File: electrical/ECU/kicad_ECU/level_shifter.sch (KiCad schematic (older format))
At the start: 24 parts

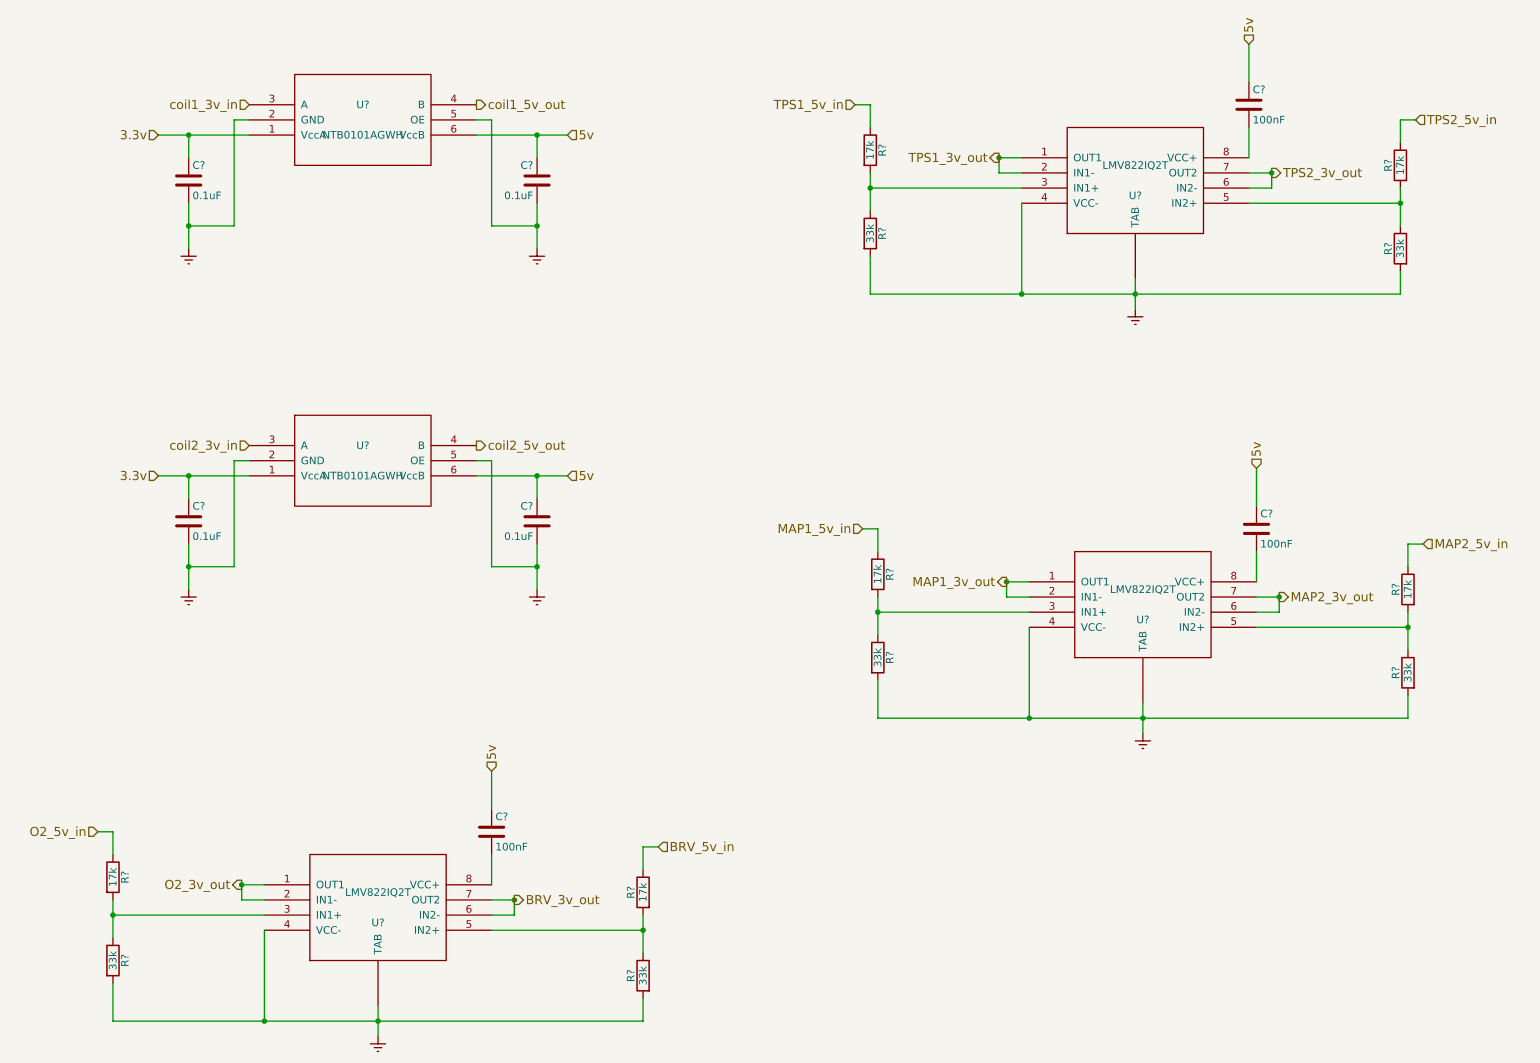
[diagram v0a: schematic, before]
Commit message: fixed some naming errors and initial round of double checking
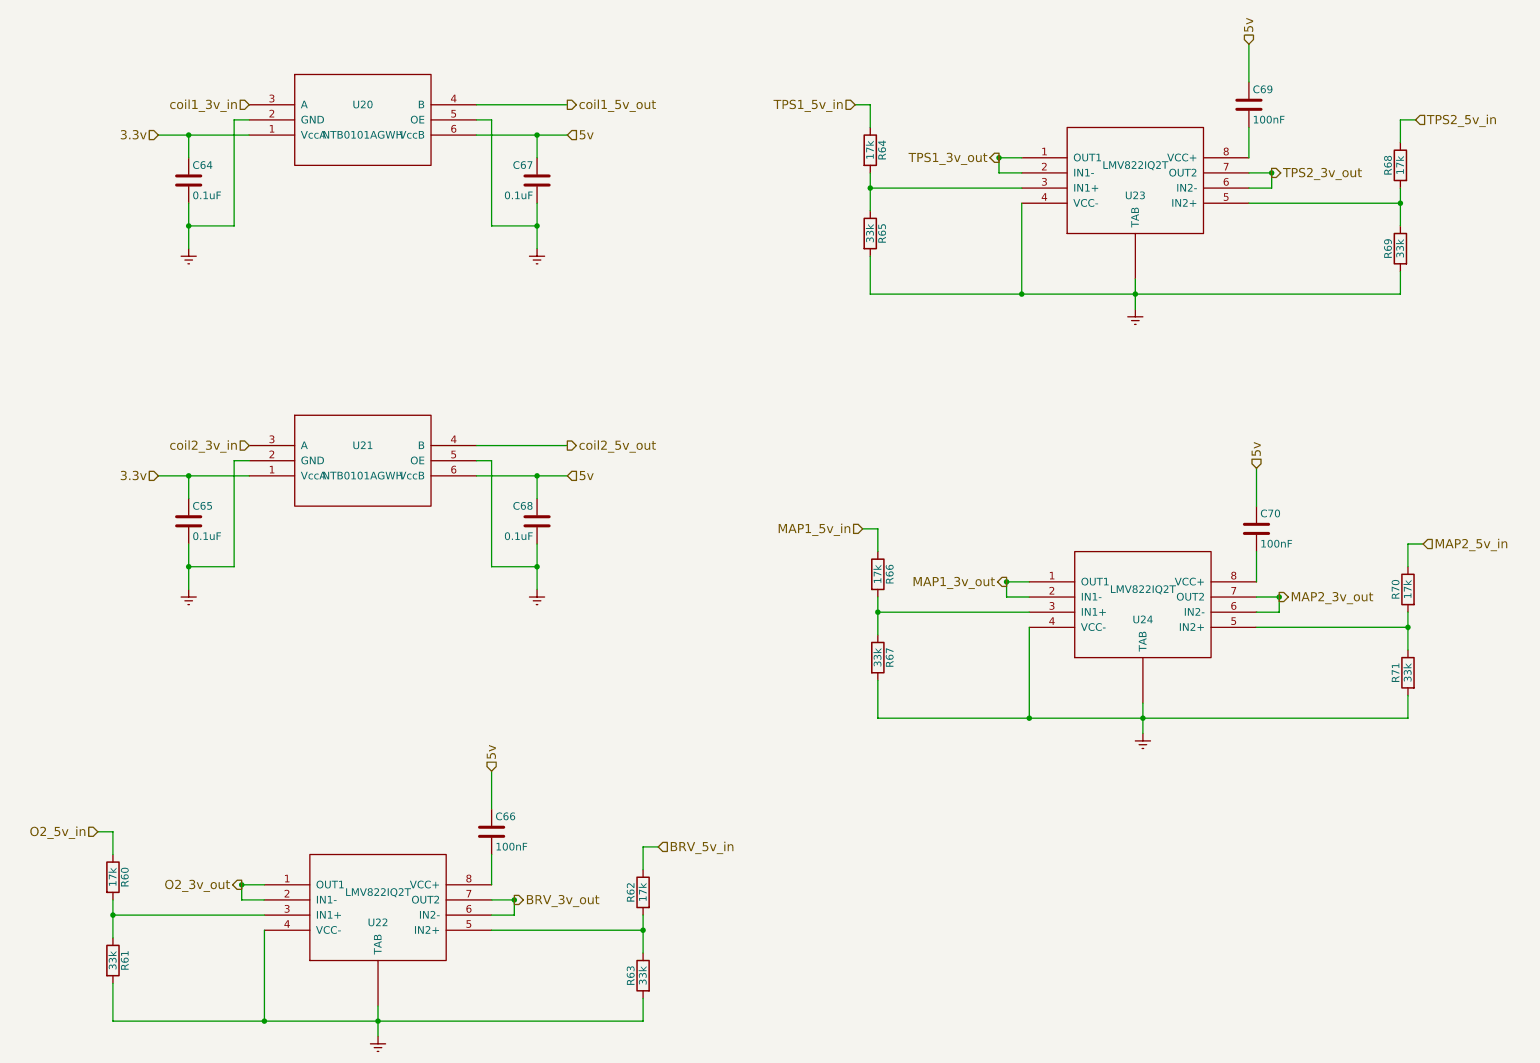
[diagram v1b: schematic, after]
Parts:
- gave numbers to parts that had none: 24
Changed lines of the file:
@@
 $Descr A4 11693 8268
 encoding utf-8
-Sheet 21 33
+Sheet 25 33
 Title "Level shifter 3.3v <-> 5v"
 Date ""
@@
 Text HLabel 9400 1650 2    60   Output ~ 0
 TPS2_3v_out
-Text HLabel 4150 1200 2    60   Output ~ 0
+Text HLabel 4750 1200 2    60   Output ~ 0
 coil1_5v_out
-Text HLabel 4150 3450 2    60   Output ~ 0
+Text HLabel 4750 3450 2    60   Output ~ 0
 coil2_5v_out
 $Comp
-L LMV822IQ2T U?
+L LMV822IQ2T U23
 U 1 1 597915F5
 P 8500 1700
-F 0 "U?" H 8500 1600 50  0000 C CNN
+F 0 "U23" H 8500 1600 50  0000 C CNN
 F 1 "LMV822IQ2T" H 8500 1800 50  0000 C CNN
 F 2 "MODULE" H 8500 1700 50  0001 C CNN
@@
 $EndComp
 $Comp
-L Earth #PWR?
+L Earth #PWR64
 U 1 1 597916F8
 P 8500 2550
-F 0 "#PWR?" H 8500 2300 50  0001 C CNN
+F 0 "#PWR64" H 8500 2300 50  0001 C CNN
 F 1 "Earth" H 8500 2400 50  0001 C CNN
 F 2 "" H 8500 2550 50  0001 C CNN
@@
 $EndComp
 $Comp
-L R R?
+L R R64
 U 1 1 59791774
 P 6750 1500
-F 0 "R?" V 6830 1500 50  0000 C CNN
+F 0 "R64" V 6830 1500 50  0000 C CNN
 F 1 "17k" V 6750 1500 50  0000 C CNN
 F 2 "" V 6680 1500 50  0001 C CNN
@@
 $EndComp
 $Comp
-L R R?
+L R R65
 U 1 1 5979178D
 P 6750 2050
-F 0 "R?" V 6830 2050 50  0000 C CNN
+F 0 "R65" V 6830 2050 50  0000 C CNN
 F 1 "33k" V 6750 2050 50  0000 C CNN
 F 2 "" V 6680 2050 50  0001 C CNN
@@
 $EndComp
 $Comp
-L C C?
+L C C69
 U 1 1 597917D3
 P 9250 1200
-F 0 "C?" H 9275 1300 50  0000 L CNN
+F 0 "C69" H 9275 1300 50  0000 L CNN
 F 1 "100nF" H 9275 1100 50  0000 L CNN
 F 2 "" H 9288 1050 50  0001 C CNN
@@
 Connection ~ 7750 2450
 $Comp
-L R R?
+L R R68
 U 1 1 59791914
 P 10250 1600
-F 0 "R?" V 10330 1600 50  0000 C CNN
+F 0 "R68" V 10330 1600 50  0000 C CNN
 F 1 "17k" V 10250 1600 50  0000 C CNN
 F 2 "" V 10180 1600 50  0001 C CNN
@@
 $EndComp
 $Comp
-L R R?
+L R R69
 U 1 1 5979191A
 P 10250 2150
-F 0 "R?" V 10330 2150 50  0000 C CNN
+F 0 "R69" V 10330 2150 50  0000 C CNN
 F 1 "33k" V 10250 2150 50  0000 C CNN
 F 2 "" V 10180 2150 50  0001 C CNN
@@
 MAP2_3v_out
 $Comp
-L LMV822IQ2T U?
+L LMV822IQ2T U24
 U 1 1 59791C46
 P 8550 4500
-F 0 "U?" H 8550 4400 50  0000 C CNN
+F 0 "U24" H 8550 4400 50  0000 C CNN
 F 1 "LMV822IQ2T" H 8550 4600 50  0000 C CNN
 F 2 "MODULE" H 8550 4500 50  0001 C CNN
@@
 $EndComp
 $Comp
-L Earth #PWR?
+L Earth #PWR65
 U 1 1 59791C4C
 P 8550 5350
-F 0 "#PWR?" H 8550 5100 50  0001 C CNN
+F 0 "#PWR65" H 8550 5100 50  0001 C CNN
 F 1 "Earth" H 8550 5200 50  0001 C CNN
 F 2 "" H 8550 5350 50  0001 C CNN
@@
 $EndComp
 $Comp
-L R R?
+L R R66
 U 1 1 59791C52
 P 6800 4300
-F 0 "R?" V 6880 4300 50  0000 C CNN
+F 0 "R66" V 6880 4300 50  0000 C CNN
 F 1 "17k" V 6800 4300 50  0000 C CNN
 F 2 "" V 6730 4300 50  0001 C CNN
@@
 $EndComp
 $Comp
-L R R?
+L R R67
 U 1 1 59791C58
 P 6800 4850
-F 0 "R?" V 6880 4850 50  0000 C CNN
+F 0 "R67" V 6880 4850 50  0000 C CNN
 F 1 "33k" V 6800 4850 50  0000 C CNN
 F 2 "" V 6730 4850 50  0001 C CNN
@@
 $EndComp
 $Comp
-L C C?
+L C C70
 U 1 1 59791C5E
 P 9300 4000
-F 0 "C?" H 9325 4100 50  0000 L CNN
+F 0 "C70" H 9325 4100 50  0000 L CNN
 F 1 "100nF" H 9325 3900 50  0000 L CNN
 F 2 "" H 9338 3850 50  0001 C CNN
@@
 Connection ~ 7800 5250
 $Comp
-L R R?
+L R R70
 U 1 1 59791C79
 P 10300 4400
-F 0 "R?" V 10380 4400 50  0000 C CNN
+F 0 "R70" V 10380 4400 50  0000 C CNN
 F 1 "17k" V 10300 4400 50  0000 C CNN
 F 2 "" V 10230 4400 50  0001 C CNN
@@
 $EndComp
 $Comp
-L R R?
+L R R71
 U 1 1 59791C7F
 P 10300 4950
-F 0 "R?" V 10380 4950 50  0000 C CNN
+F 0 "R71" V 10380 4950 50  0000 C CNN
 F 1 "33k" V 10300 4950 50  0000 C CNN
 F 2 "" V 10230 4950 50  0001 C CNN
@@
 BRV_3v_out
 $Comp
-L LMV822IQ2T U?
+L LMV822IQ2T U22
 U 1 1 59791E5C
 P 3500 6500
-F 0 "U?" H 3500 6400 50  0000 C CNN
+F 0 "U22" H 3500 6400 50  0000 C CNN
 F 1 "LMV822IQ2T" H 3500 6600 50  0000 C CNN
 F 2 "MODULE" H 3500 6500 50  0001 C CNN
@@
 $EndComp
 $Comp
-L Earth #PWR?
+L Earth #PWR61
 U 1 1 59791E62
 P 3500 7350
-F 0 "#PWR?" H 3500 7100 50  0001 C CNN
+F 0 "#PWR61" H 3500 7100 50  0001 C CNN
 F 1 "Earth" H 3500 7200 50  0001 C CNN
 F 2 "" H 3500 7350 50  0001 C CNN
@@
 $EndComp
 $Comp
-L R R?
+L R R60
 U 1 1 59791E68
 P 1750 6300
-F 0 "R?" V 1830 6300 50  0000 C CNN
+F 0 "R60" V 1830 6300 50  0000 C CNN
 F 1 "17k" V 1750 6300 50  0000 C CNN
 F 2 "" V 1680 6300 50  0001 C CNN
@@
 $EndComp
 $Comp
-L R R?
+L R R61
 U 1 1 59791E6E
 P 1750 6850
-F 0 "R?" V 1830 6850 50  0000 C CNN
+F 0 "R61" V 1830 6850 50  0000 C CNN
 F 1 "33k" V 1750 6850 50  0000 C CNN
 F 2 "" V 1680 6850 50  0001 C CNN
@@
 $EndComp
 $Comp
-L C C?
+L C C66
 U 1 1 59791E74
 P 4250 6000
-F 0 "C?" H 4275 6100 50  0000 L CNN
+F 0 "C66" H 4275 6100 50  0000 L CNN
 F 1 "100nF" H 4275 5900 50  0000 L CNN
 F 2 "" H 4288 5850 50  0001 C CNN
@@
 Connection ~ 2750 7250
 $Comp
-L R R?
+L R R62
 U 1 1 59791E8F
 P 5250 6400
-F 0 "R?" V 5330 6400 50  0000 C CNN
+F 0 "R62" V 5330 6400 50  0000 C CNN
 F 1 "17k" V 5250 6400 50  0000 C CNN
 F 2 "" V 5180 6400 50  0001 C CNN
@@
 $EndComp
 $Comp
-L R R?
+L R R63
 U 1 1 59791E95
 P 5250 6950
-F 0 "R?" V 5330 6950 50  0000 C CNN
+F 0 "R63" V 5330 6950 50  0000 C CNN
 F 1 "33k" V 5250 6950 50  0000 C CNN
 F 2 "" V 5180 6950 50  0001 C CNN
@@
 Connection ~ 4400 6450
 $Comp
-L NTB0101AGWH U?
+L NTB0101AGWH U20
 U 1 1 5979207E
 P 3400 1300
-F 0 "U?" H 3400 1200 50  0000 C CNN
+F 0 "U20" H 3400 1200 50  0000 C CNN
 F 1 "NTB0101AGWH" H 3400 1400 50  0000 C CNN
 F 2 "MODULE" H 3400 1300 50  0001 C CNN
@@
 $EndComp
 $Comp
-L C C?
+L C C64
 U 1 1 59792109
 P 2250 1700
-F 0 "C?" H 2275 1800 50  0000 L CNN
+F 0 "C64" H 2275 1800 50  0000 L CNN
 F 1 "0.1uF" H 2275 1600 50  0000 L CNN
 F 2 "" H 2288 1550 50  0001 C CNN
@@
 $EndComp
 $Comp
-L Earth #PWR?
+L Earth #PWR59
 U 1 1 5979219D
 P 2250 2150
-F 0 "#PWR?" H 2250 1900 50  0001 C CNN
+F 0 "#PWR59" H 2250 1900 50  0001 C CNN
 F 1 "Earth" H 2250 2000 50  0001 C CNN
 F 2 "" H 2250 2150 50  0001 C CNN
@@
 Connection ~ 2250 2000
 $Comp
-L C C?
+L C C67
 U 1 1 597926F6
 P 4550 1700
-F 0 "C?" H 4575 1800 50  0000 L CNN
+F 0 "C67" H 4575 1800 50  0000 L CNN
 F 1 "0.1uF" H 4575 1600 50  0000 L CNN
 F 2 "" H 4588 1550 50  0001 C CNN
@@
 $EndComp
 $Comp
-L Earth #PWR?
+L Earth #PWR62
 U 1 1 597926FC
 P 4550 2150
-F 0 "#PWR?" H 4550 1900 50  0001 C CNN
+F 0 "#PWR62" H 4550 1900 50  0001 C CNN
 F 1 "Earth" H 4550 2000 50  0001 C CNN
 F 2 "" H 4550 2150 50  0001 C CNN
@@
 Connection ~ 4550 2000
 $Comp
-L NTB0101AGWH U?
+L NTB0101AGWH U21
 U 1 1 597928D1
 P 3400 3550
-F 0 "U?" H 3400 3450 50  0000 C CNN
+F 0 "U21" H 3400 3450 50  0000 C CNN
 F 1 "NTB0101AGWH" H 3400 3650 50  0000 C CNN
 F 2 "MODULE" H 3400 3550 50  0001 C CNN
@@
 $EndComp
 $Comp
-L C C?
+L C C65
 U 1 1 597928D7
 P 2250 3950
-F 0 "C?" H 2275 4050 50  0000 L CNN
+F 0 "C65" H 2275 4050 50  0000 L CNN
 F 1 "0.1uF" H 2275 3850 50  0000 L CNN
 F 2 "" H 2288 3800 50  0001 C CNN
@@
 $EndComp
 $Comp
-L Earth #PWR?
+L Earth #PWR60
 U 1 1 597928DD
 P 2250 4400
-F 0 "#PWR?" H 2250 4150 50  0001 C CNN
+F 0 "#PWR60" H 2250 4150 50  0001 C CNN
 F 1 "Earth" H 2250 4250 50  0001 C CNN
 F 2 "" H 2250 4400 50  0001 C CNN
@@
 Connection ~ 2250 4250
 $Comp
-L C C?
+L C C68
 U 1 1 597928ED
 P 4550 3950
-F 0 "C?" H 4575 4050 50  0000 L CNN
+F 0 "C68" H 4575 4050 50  0000 L CNN
 F 1 "0.1uF" H 4575 3850 50  0000 L CNN
 F 2 "" H 4588 3800 50  0001 C CNN
@@
 $EndComp
 $Comp
-L Earth #PWR?
+L Earth #PWR63
 U 1 1 597928F3
 P 4550 4400
-F 0 "#PWR?" H 4550 4150 50  0001 C CNN
+F 0 "#PWR63" H 4550 4150 50  0001 C CNN
 F 1 "Earth" H 4550 4250 50  0001 C CNN
 F 2 "" H 4550 4400 50  0001 C CNN
@@
 	4250 4250 4550 4250
 Connection ~ 4550 4250
+Wire Wire Line
+	4150 1200 4750 1200
+Wire Wire Line
+	4150 3450 4750 3450
 $EndSCHEMATC
